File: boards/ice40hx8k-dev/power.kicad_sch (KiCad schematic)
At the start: 17 parts, among them U1 ICE40HX8K-CT256

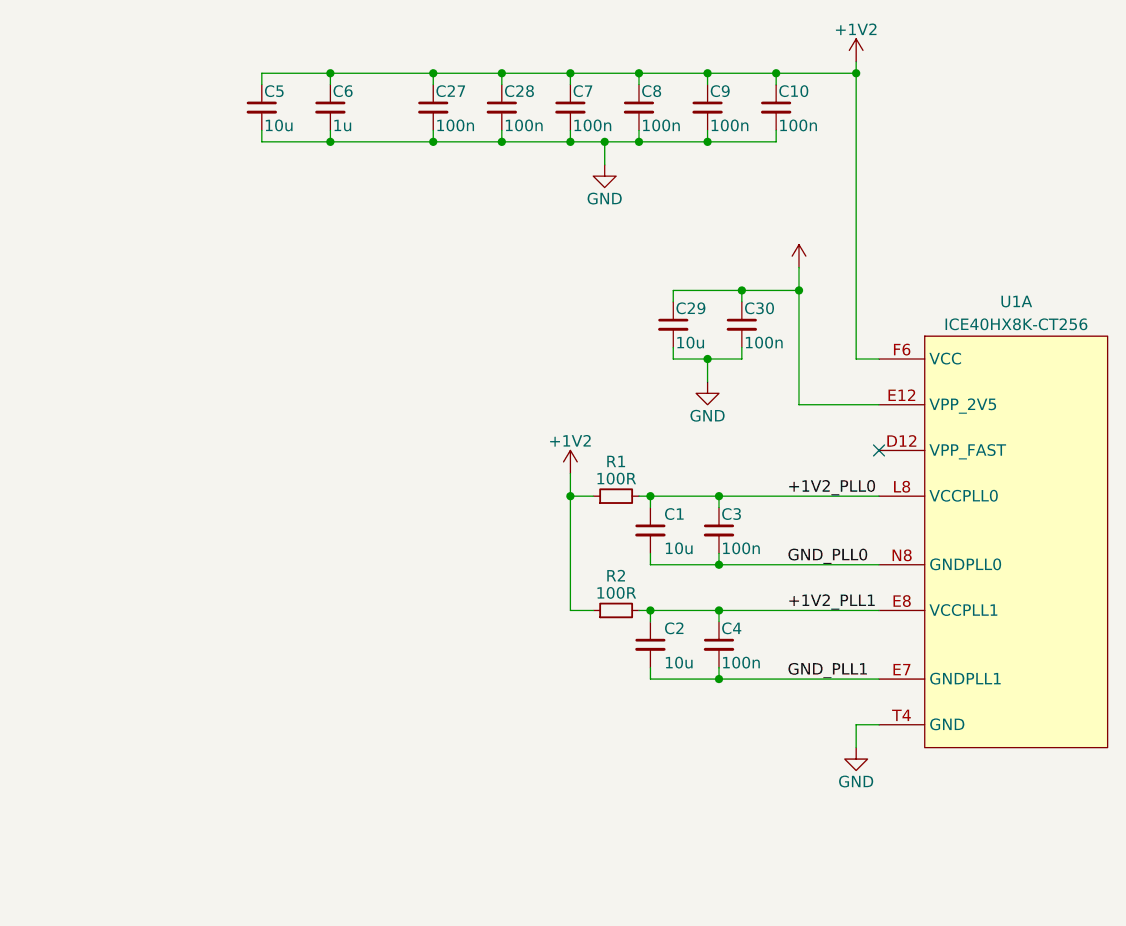
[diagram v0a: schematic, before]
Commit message: Fan out all signal pads.
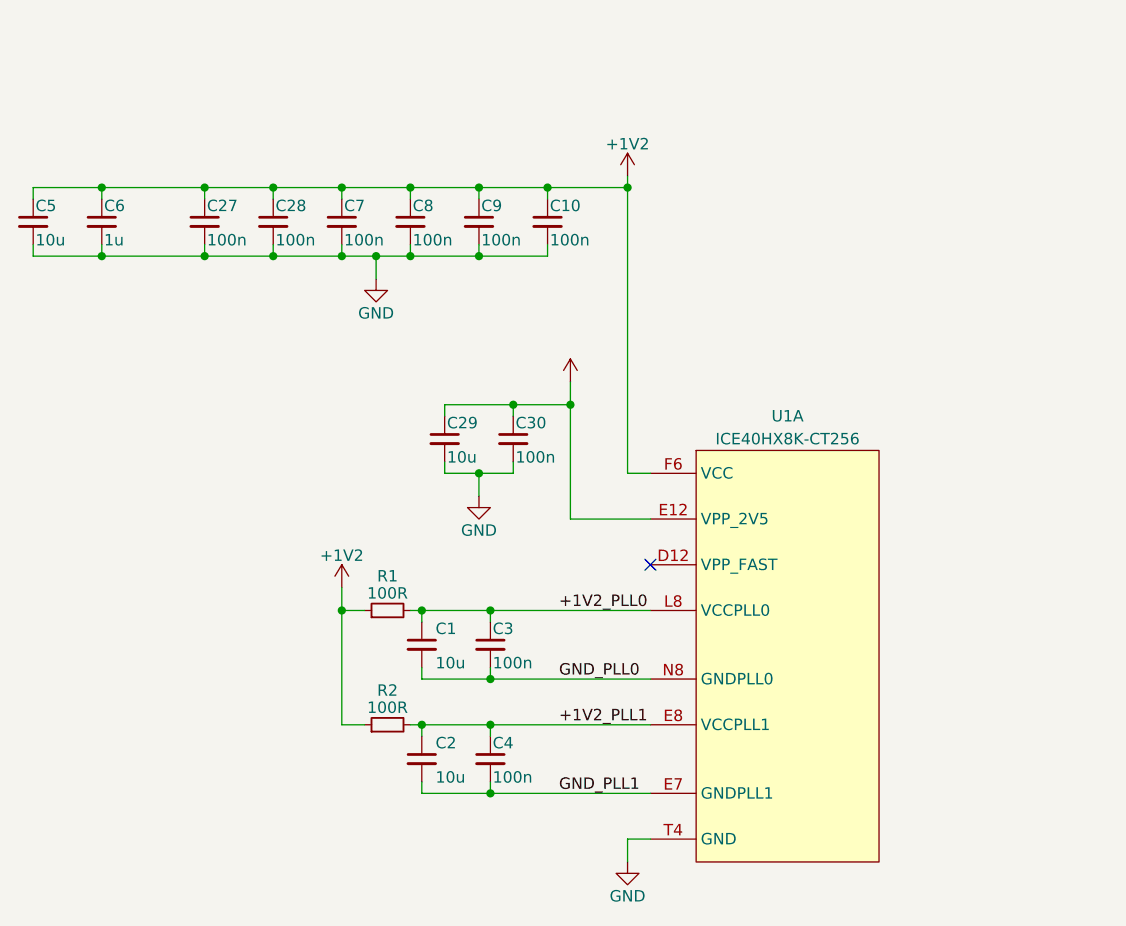
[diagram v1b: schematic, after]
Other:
- moved on the sheet: C1, C10, C2, C27, C28, C29, C3, C30, C4, C5, C6, C7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
